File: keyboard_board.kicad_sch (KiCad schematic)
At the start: 17 parts, among them J1 Conn_02x20_Odd_Even, J2 Trackpad Connector, J3 Rp500KB, J4 USB_C_Receptacle_USB2.0_16P, P1 S2B-PH-SM4-TB, P2 S2B-PH-SM4-TB, SW1 Reset, U1 SC0915, U2 74HC165, U3 74HC165, U4 LM66100DCK

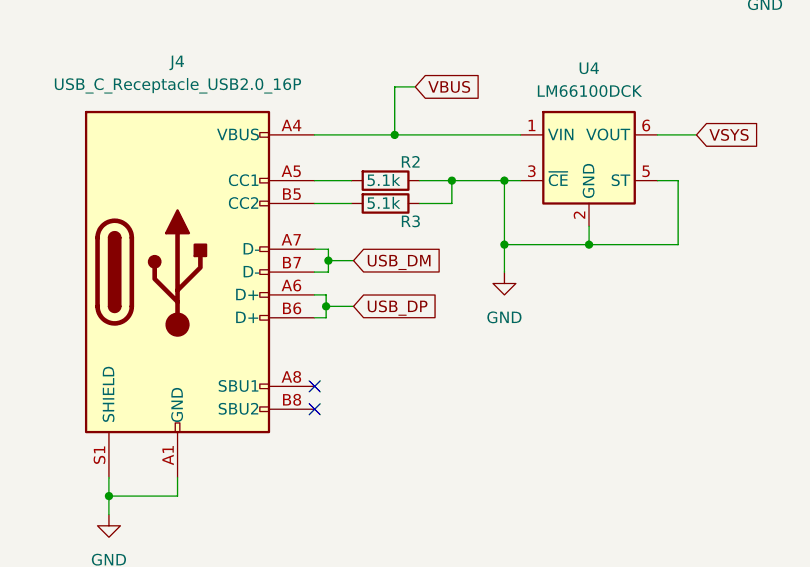
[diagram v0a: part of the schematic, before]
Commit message: -Changes USB labels to support differential pair - Does some major layout changes.
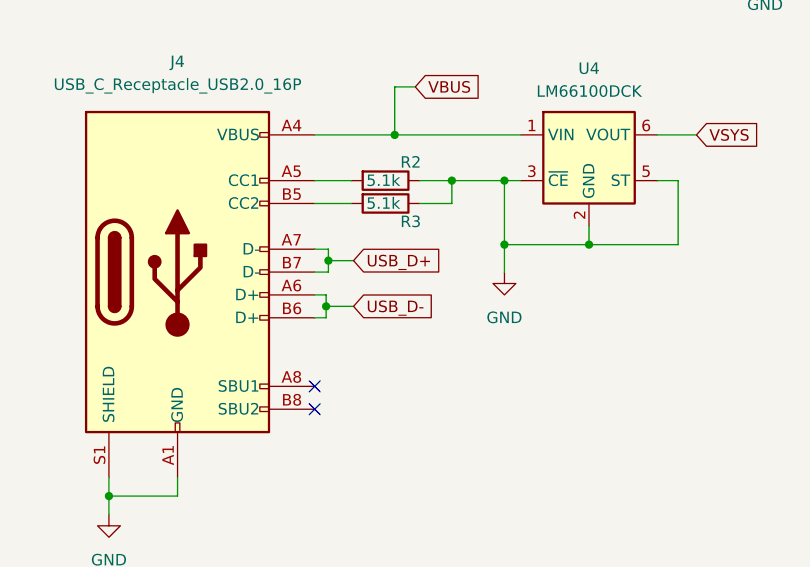
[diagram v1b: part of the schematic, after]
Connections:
- net USB_DM: no longer J4.A7 (D-), J4.B7 (D-)
- net USB_DP: no longer J4.A6 (D+), J4.B6 (D+)
- new net USB_D+: J4.A7 (D-), J4.B7 (D-)
- new net USB_D-: J4.A6 (D+), J4.B6 (D+)
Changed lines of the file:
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@@
 		)
 	)
-	(global_label "USB_DP"
+	(global_label "USB_D-"
 		(shape input)
 		(at 49.53 166.878 0)
@@
 		)
 		(property "Intersheetrefs" "${INTERSHEET_REFS}"
-			(at 59.8328 166.878 0)
+			(at 60.1352 166.878 0)
 			(effects
 				(font
@@
 		)
 	)
-	(global_label "USB_DM"
+	(global_label "USB_D+"
 		(shape input)
 		(at 49.53 161.798 0)
@@
 		)
 		(property "Intersheetrefs" "${INTERSHEET_REFS}"
-			(at 60.0142 161.798 0)
+			(at 60.1352 161.798 0)
 			(effects
 				(font
@@
 		(exclude_from_sim no)
 		(in_bom yes)
-		(on_board yes)
+		(on_board no)
 		(dnp no)
 		(fields_autoplaced yes)
@@
 		(exclude_from_sim no)
 		(in_bom yes)
-		(on_board yes)
+		(on_board no)
 		(dnp no)
 		(property "Reference" "R2"
@@
 		(exclude_from_sim no)
 		(in_bom yes)
-		(on_board yes)
+		(on_board no)
 		(dnp no)
 		(fields_autoplaced yes)
@@
 		(exclude_from_sim no)
 		(in_bom yes)
-		(on_board yes)
+		(on_board no)
 		(dnp no)
 		(property "Reference" "R3"

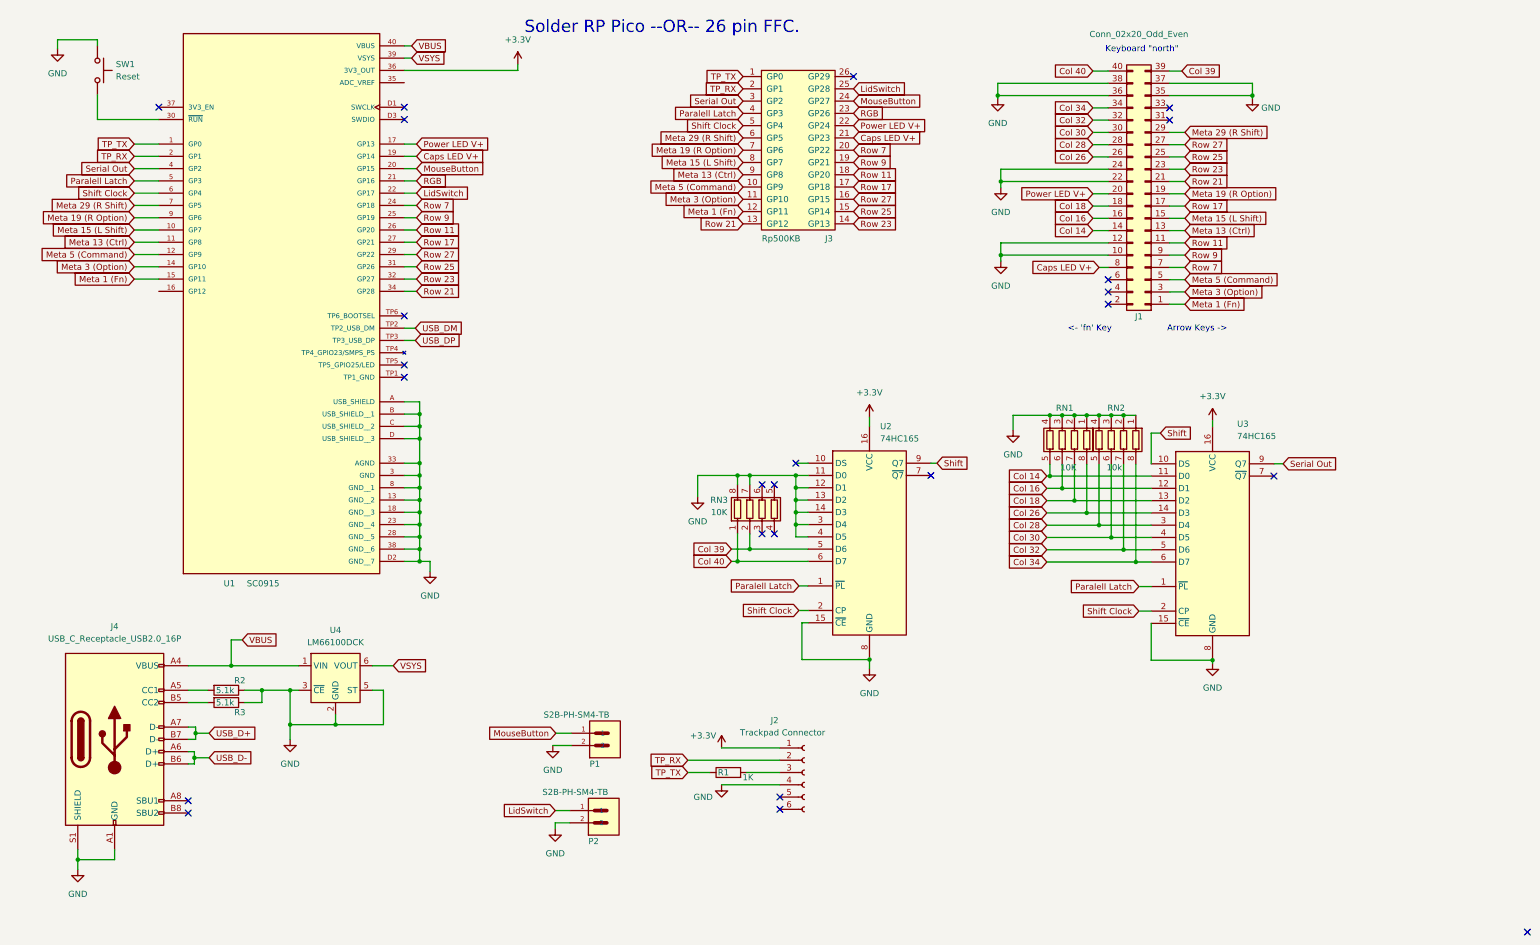
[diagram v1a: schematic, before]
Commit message: Adds Power input 2-pin JST PH. Adds RGB output Adds Power Button input
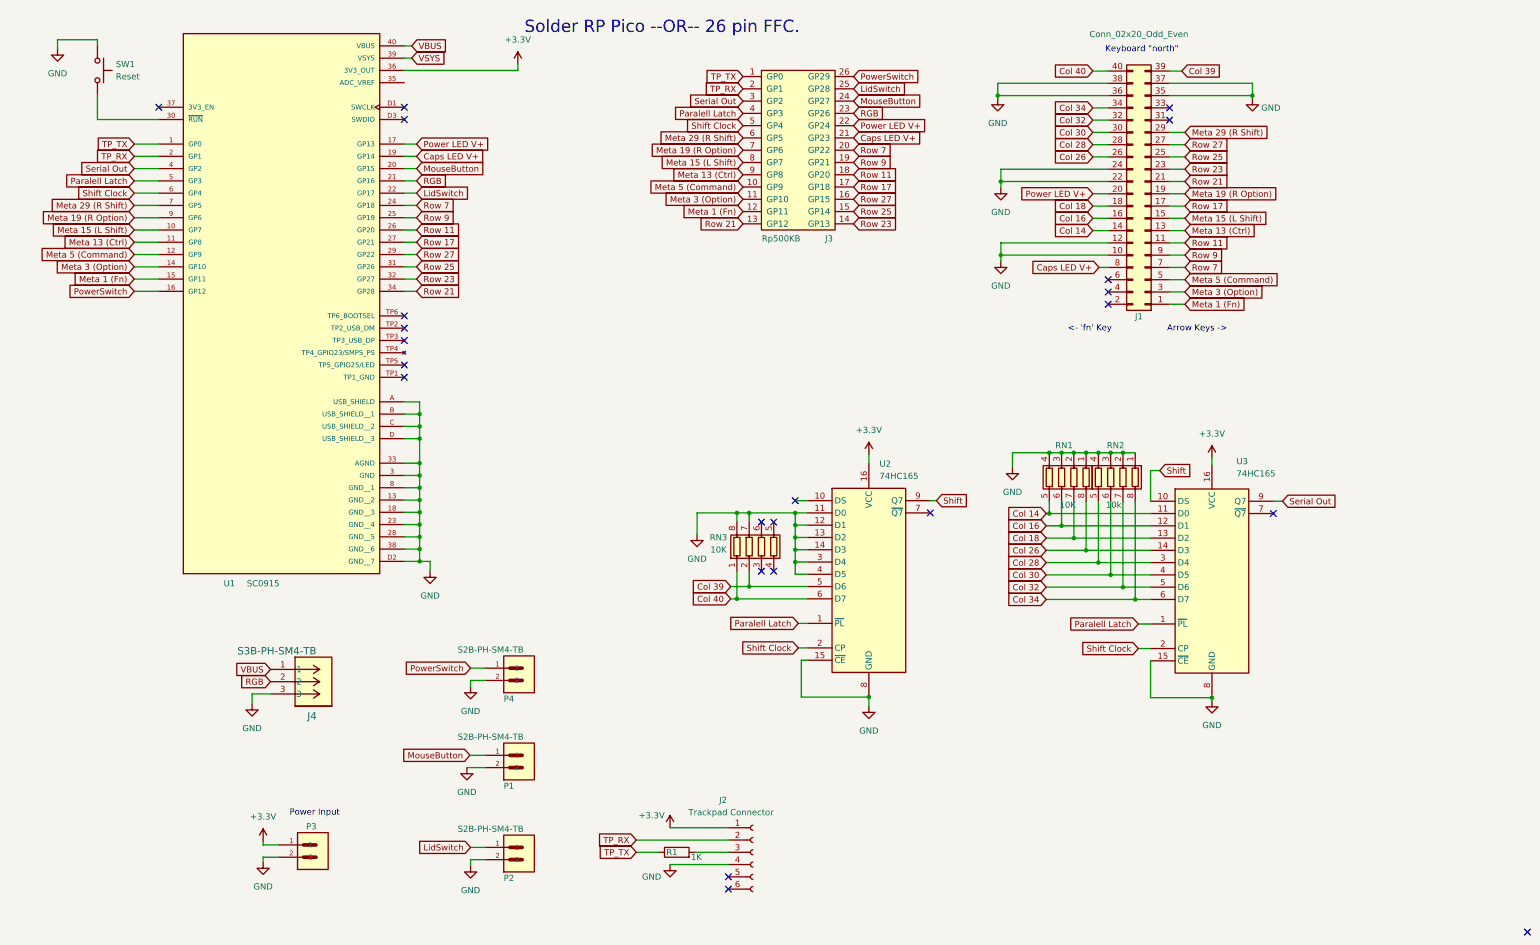
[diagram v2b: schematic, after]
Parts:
- removed J4: USB_C_Receptacle_USB2.0_16P, Aaron:GCT_USB4105-GF-A, symbol Connector:USB_C_Receptacle_USB2.0_16P
- removed R2, R3: 5.1k, Resistor_SMD:R_0805_2012Metric, symbol Device:R
- removed U4: LM66100DCK, Package_TO_SOT_SMD:SOT-363_SC-70-6, symbol Power_Management:LM66100DCK
- added J4: S3B-PH-SM4-TB, Aaron:CONN3_S3B-PH_JST, symbol Aaron:S3B-PH-SM4-TB
- added P3, P4: S2B-PH-SM4-TB, Aaron:JST_S2B-PH-SM4-TB, symbol Aaron:S2B-PH-SM4-TB
- J3: footprint Connector_FFC-FPC:Molex_200528-0260_1x26-1MP_P1.00mm_Horizontal -> Aaron:AMPHENOL_F52R-1A7H1-11026
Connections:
- net +3.3V: now also P3.1
- net GND: now also J4.3, P3.2, P4.2
- net RGB: now also J4.2
- net VBUS: now also J4.1
- net PowerSwitch: now reaches J3.26 (GP29)
- net PowerSwitch: now also U1.16 (GP12), P4.1
- net USB_DM: no longer names the net of U1.TP2 (TP2_USB_DM)
- net USB_DP: no longer names the net of U1.TP3 (TP3_USB_DP)
- no-connect marks 24 -> 23
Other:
- note added: "Power Input"
- moved on the sheet: J2, P1, P2, R1, RN1, RN2, RN3, U2, U3

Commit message: Completes Pico version
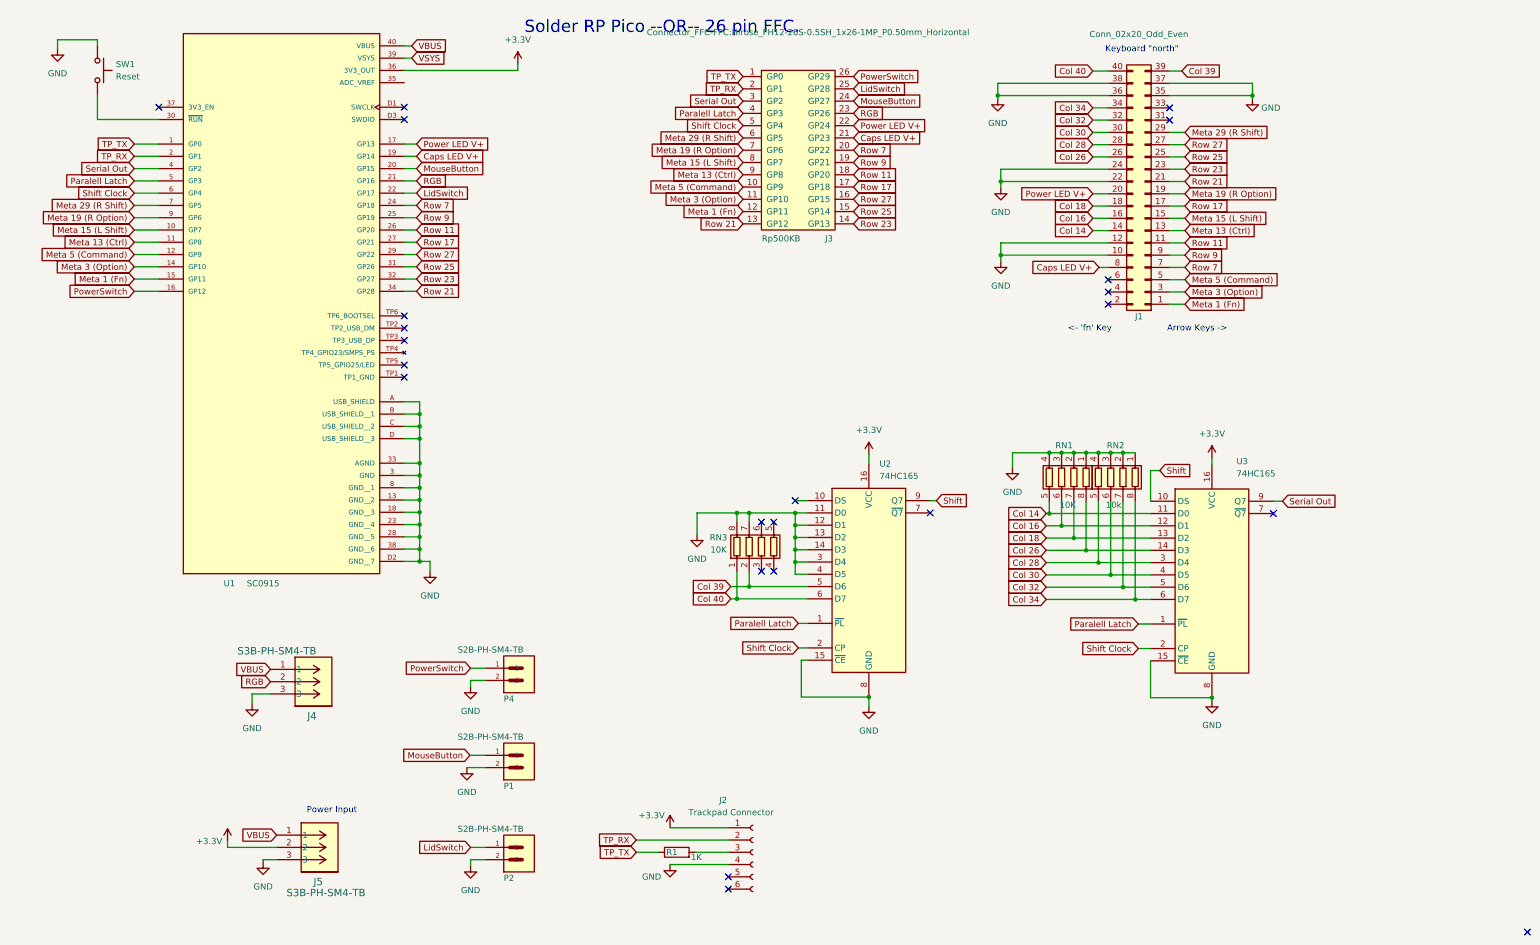
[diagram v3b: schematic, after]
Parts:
- removed P3: S2B-PH-SM4-TB, Aaron:JST_S2B-PH-SM4-TB, symbol Aaron:S2B-PH-SM4-TB
- added J5: S3B-PH-SM4-TB, Aaron:CONN3_S3B-PH_JST, symbol Aaron:S3B-PH-SM4-TB
- J3: footprint Aaron:AMPHENOL_F52R-1A7H1-11026 -> Connector_FFC-FPC:Hirose_FH12-26S-0.5SH_1x26-1MP_P0.50mm_Horizontal
- SW1: footprint (none) -> Aaron:SW4_PTS815 SJM 250 SMTR LFS_CNK
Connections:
- net +3.3V: now also J5.2
- net GND: now also J5.3
- net VBUS: now also J5.1
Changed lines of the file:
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@@
 	(generator_version "8.0")
 	(paper "A4")
+	(title_block
+		(date "2025-03-18")
+		(rev "1.0")
+	)
 	(junction
 		(at 231.013 123.952)
@@
 	(wire
 		(pts
-			(xy 64.008 184.912) (xy 60.706 184.912)
+			(xy 63.5 185.42) (xy 53.34 185.42)
 		)
 		(stroke
@@
 	(wire
 		(pts
-			(xy 60.706 187.452) (xy 60.706 188.468)
+			(xy 60.706 187.96) (xy 60.706 188.468)
 		)
 		(stroke
@@
 	(wire
 		(pts
-			(xy 60.706 184.912) (xy 60.706 184.15)
+			(xy 53.34 185.42) (xy 53.34 184.15)
 		)
 		(stroke
@@
 	(wire
 		(pts
-			(xy 64.008 187.452) (xy 60.706 187.452)
+			(xy 63.5 187.96) (xy 60.706 187.96)
 		)
 		(stroke
@@
 	(text "Power Input"
 		(exclude_from_sim no)
-		(at 71.374 178.308 0)
+		(at 74.93 177.8 0)
 		(effects
 			(font
@@
 		)
 	)
+	(global_label "VBUS"
+		(shape input)
+		(at 63.5 182.88 180)
+		(fields_autoplaced yes)
+		(effects
+			(font
+				(size 1.27 1.27)
+			)
+			(justify right)
+		)
+		(property "Intersheetrefs" "${INTERSHEET_REFS}"
+			(at 55.6162 182.88 0)
+			(effects
+				(font
+					(size 1.27 1.27)
+				)
+				(justify right)
+				(hide yes)
+			)
+		)
+	)
 	(global_label "Meta 1 (Fn)"
 		(shape input)
@@
 			)
 		)
-		(property "Footprint" "Aaron:AMPHENOL_F52R-1A7H1-11026"
+		(property "Footprint" "Connector_FFC-FPC:Hirose_FH12-26S-0.5SH_1x26-1MP_P0.50mm_Horizontal"
 			(at 173.482 16.764 0)
 			(effects
@@
 					(size 1.27 1.27)
 				)
-				(hide yes)
 			)
 		)
@@
 	)
 	(symbol
-		(lib_id "Aaron:S2B-PH-SM4-TB")
-		(at 69.088 186.182 0)
-		(unit 1)
-		(exclude_from_sim no)
-		(in_bom yes)
-		(on_board yes)
-		(dnp no)
-		(property "Reference" "P3"
-			(at 69.596 181.102 0)
-			(effects
-				(font
-					(size 1.27 1.27)
-				)
-				(justify left)
-			)
-		)
-		(property "Value" "S2B-PH-SM4-TB"
-			(at 58.293 181.102 0)
-			(effects
-				(font
-					(size 1.27 1.27)
-				)
-				(justify left)
-				(hide yes)
-			)
-		)
-		(property "Footprint" "Aaron:JST_S2B-PH-SM4-TB"
-			(at 69.088 186.182 0)
-			(effects
-				(font
-					(size 1.27 1.27)
-				)
-				(justify bottom)
-				(hide yes)
-			)
-		)
-		(property "Datasheet" ""
-			(at 69.088 186.182 0)
-			(effects
-				(font
-					(size 1.27 1.27)
-				)
-				(hide yes)
-			)
-		)
-		(property "Description" "Power Input"
-			(at 69.088 186.182 0)
-			(effects
-				(font
-					(size 1.27 1.27)
-				)
-				(hide yes)
-			)
-		)
-		(property "MANUFACTURER" "JST"
-			(at 69.088 186.182 0)
-			(effects
-				(font
-					(size 1.27 1.27)
-				)
-				(justify bottom)
-				(hide yes)
-			)
-		)
-		(pin "1"
-		)
-		(pin "2"
-		)
-		(instances
-			(project "keyboard_board"
-				(path "/4c4c8fa8-6ca5-4479-92f8-c3fc64339dee"
-					(reference "P3")
-					(unit 1)
-				)
-			)
-		)
-	)
-	(symbol
 		(lib_id "power:GND")
 		(at 257.048 155.067 0)
@@
 	(symbol
 		(lib_id "power:+3.3V")
-		(at 60.706 184.15 0)
+		(at 53.34 184.15 0)
 		(unit 1)
 		(exclude_from_sim no)
@@
 		(on_board yes)
 		(dnp no)
-		(fields_autoplaced yes)
 		(property "Reference" "#PWR019"
-			(at 60.706 187.96 0)
+			(at 53.34 187.96 0)
 			(effects
 				(font
@@
 		)
 		(property "Value" "+3.3V"
-			(at 60.706 179.07 0)
+			(at 49.53 184.15 0)
 			(effects
 				(font
@@
 		)
 		(property "Footprint" ""
-			(at 60.706 184.15 0)
+			(at 53.34 184.15 0)
 			(effects
 				(font
@@
 		)
 		(property "Datasheet" ""
-			(at 60.706 184.15 0)
+			(at 53.34 184.15 0)
 			(effects
 				(font
@@
 		)
 		(property "Description" "Power symbol creates a global label with name \"+3.3V\""
-			(at 60.706 184.15 0)
+			(at 53.34 184.15 0)
 			(effects
 				(font
@@
 			)
 		)
-		(property "Footprint" ""
+		(property "Footprint" "Aaron:SW4_PTS815 SJM 250 SMTR LFS_CNK"
 			(at 31.496 24.638 0)
 			(effects
@@
 					(unit 1)
 				)
+			)
+		)
+	)
+	(symbol
+		(lib_id "Aaron:S3B-PH-SM4-TB")
+		(at 63.5 182.88 0)
+		(unit 1)
+		(exclude_from_sim no)
+		(in_bom yes)
+		(on_board yes)
+		(dnp no)
+		(property "Reference" "J5"
+			(at 71.12 192.532 0)
+			(effects
+				(font
+					(size 1.524 1.524)
+				)
+				(justify left)
+			)
+		)
+		(property "Value" "S3B-PH-SM4-TB"
+			(at 65.532 194.818 0)
+			(effects
+				(font
+					(size 1.524 1.524)
+				)
+				(justify left)
+			)
+		)
+		(property "Footprint" "Aaron:CONN3_S3B-PH_JST"
+			(at 63.5 182.88 0)
+			(effects
+				(font
+					(size 1.27 1.27)
+					(italic yes)
+				)
+				(hide yes)
+			)
+		)
+		(property "Datasheet" "S3B-PH-SM4-TB"
+			(at 63.5 182.88 0)
+			(effects
+				(font
+					(size 1.27 1.27)
+					(italic yes)
+				)
+				(hide yes)
+			)
+		)
+		(property "Description" ""
+			(at 63.5 182.88 0)
+			(effects
+				(font
+					(size 1.27 1.27)
+				)
+				(hide yes)
+			)
+		)
+		(pin "2"
+		)
+		(pin "3"
+		)
+		(pin "1"
+		)
+		(instances
+			(project "keyboard_board"
+				(path "/4c4c8fa8-6ca5-4479-92f8-c3fc64339dee"
+					(reference "J5")
+					(unit 1)
+				)

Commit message: Updates to Pico version
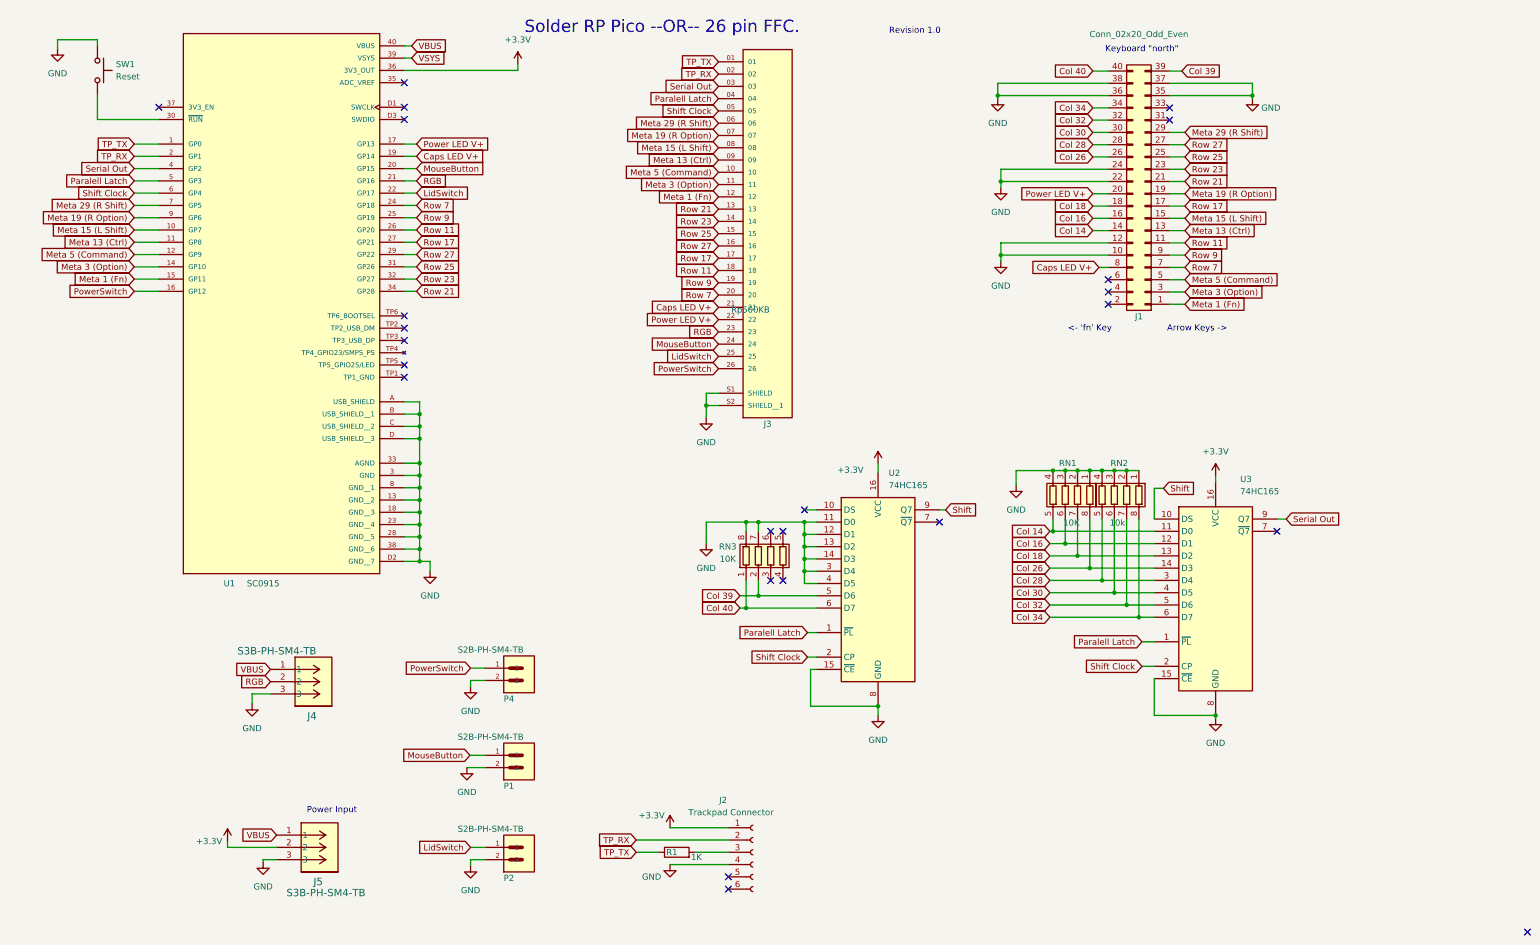
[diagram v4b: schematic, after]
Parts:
- J3: footprint Connector_FFC-FPC:Hirose_FH12-26S-0.5SH_1x26-1MP_P0.50mm_Horizontal -> Aaron:AMPHENOL_10051922-2610ELF; symbol Connector_Generic:Conn_02x13_Counter_Clockwise -> 10051922-2610ELF:10051922-2610ELF; MANUFACTURER (none) -> Amphenol; MAXIMUM_PACKAGE_HEIGHT (none) -> 3.37mm; PARTREV (none) -> J; SNAPEDA_PN (none) -> 10051922-2610ELF; STANDARD (none) -> Manufacturer Recommendations
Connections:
- net GND: now also J3.S1 (SHIELD), J3.S2 (SHIELD__1)
- net Meta 13 (Ctrl): now also J3.09; no longer J3.9 (GP8)
- net Meta 15 (L Shift): now also J3.08; no longer J3.8 (GP7)
- net Meta 19 (R Option): now also J3.07; no longer J3.7 (GP6)
- net Meta 29 (R Shift): now also J3.06; no longer J3.6 (GP5)
- net Paralell Latch: now also J3.04; no longer J3.4 (GP3)
- net Serial Out: now also J3.03; no longer J3.3 (GP2)
- net Shift Clock: now also J3.05; no longer J3.5 (GP4)
- net TP_RX: now also J3.02; no longer J3.2 (GP1)
- net TP_TX: now also J3.01; no longer J3.1 (GP0)
- no-connect marks 23 -> 24
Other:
- note added: "Revision ${REVISION}"
- moved on the sheet: RN1, RN2, RN3, U2, U3
